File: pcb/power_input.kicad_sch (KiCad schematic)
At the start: 0 parts

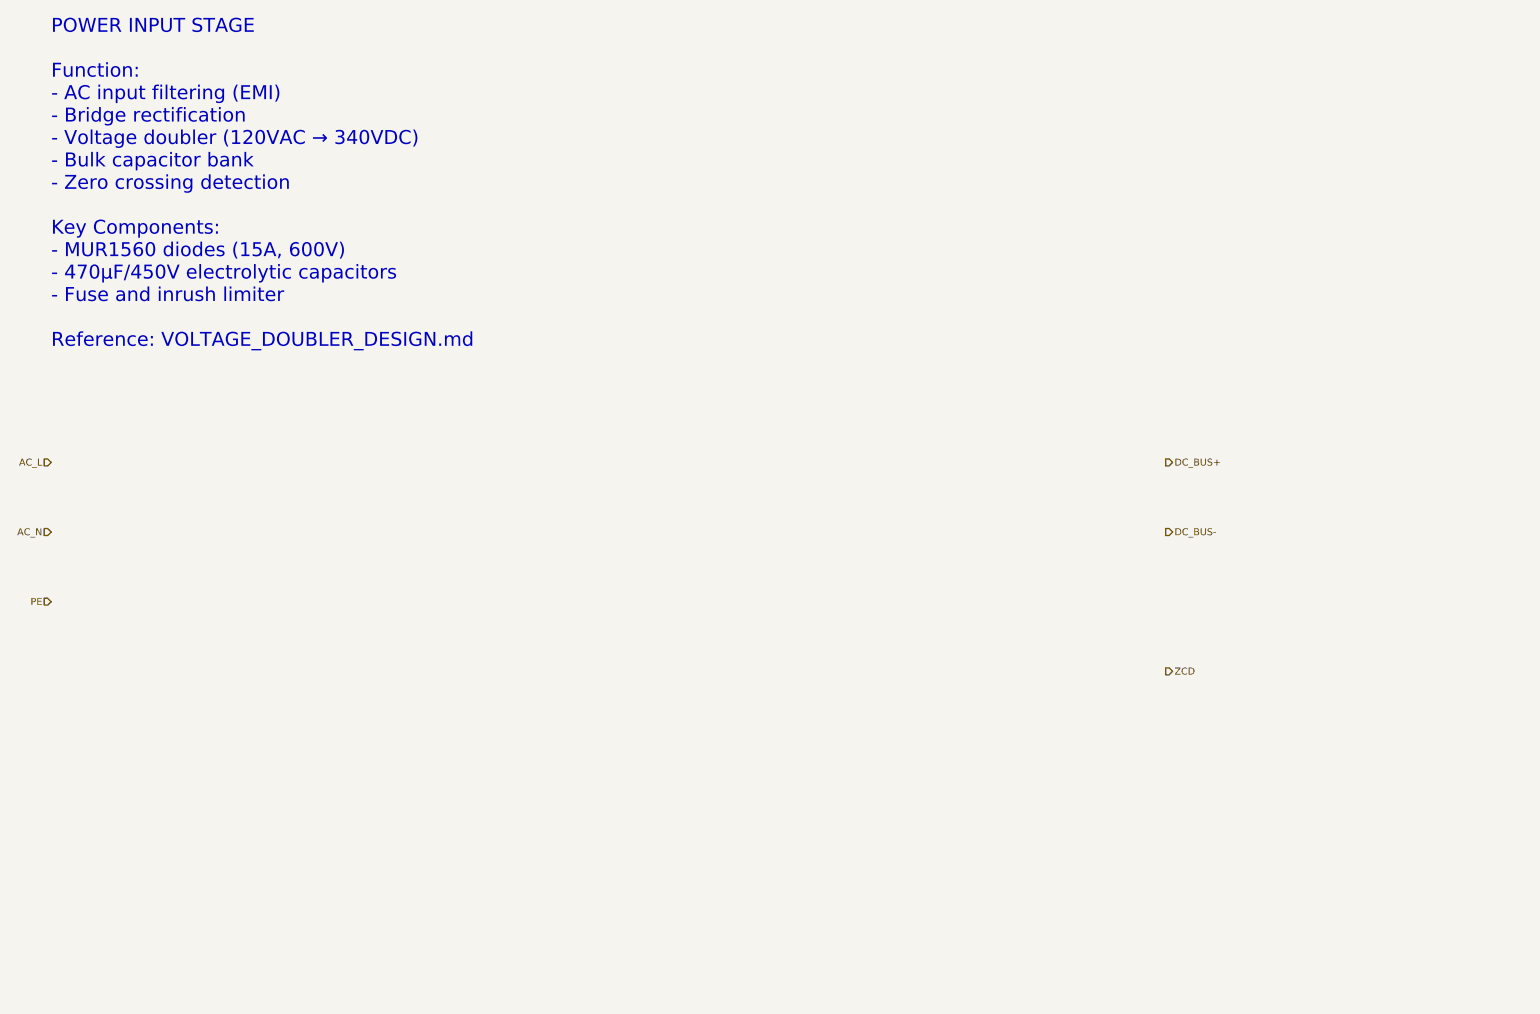
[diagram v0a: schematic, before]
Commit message: feat(pcb): populate all 7 hierarchical schematic sheets with BOM components
Schematics populated:
- half_bridge: IKW40N120H3 IGBTs, UCC21550 gate driver, bootstrap circuit
- power_input: Voltage doubler (MUR1560, 3300uF caps), NTC inrush limiter
- power_management: LMR51430 buck (36V->15V), XC6220 LDO (15V->3.3V)
- safety_interlock: TLV3201 comparators, TPS3823 watchdog, 74HC logic ICs
- sensing: MAX31865 RTD interface, ADUM1250 I2C isolator, CT burden
- mcu: ESP32-S3-WROOM-1-N4, decoupling caps, PWM RC filters, EN circuit
- user_interface: 5x fault LEDs (OCP/OVP/thermal/WDT/master), reset button

All components include MPN properties matching BOM.md specifications.
Pin assignments documented in MCU sheet for firmware reference.
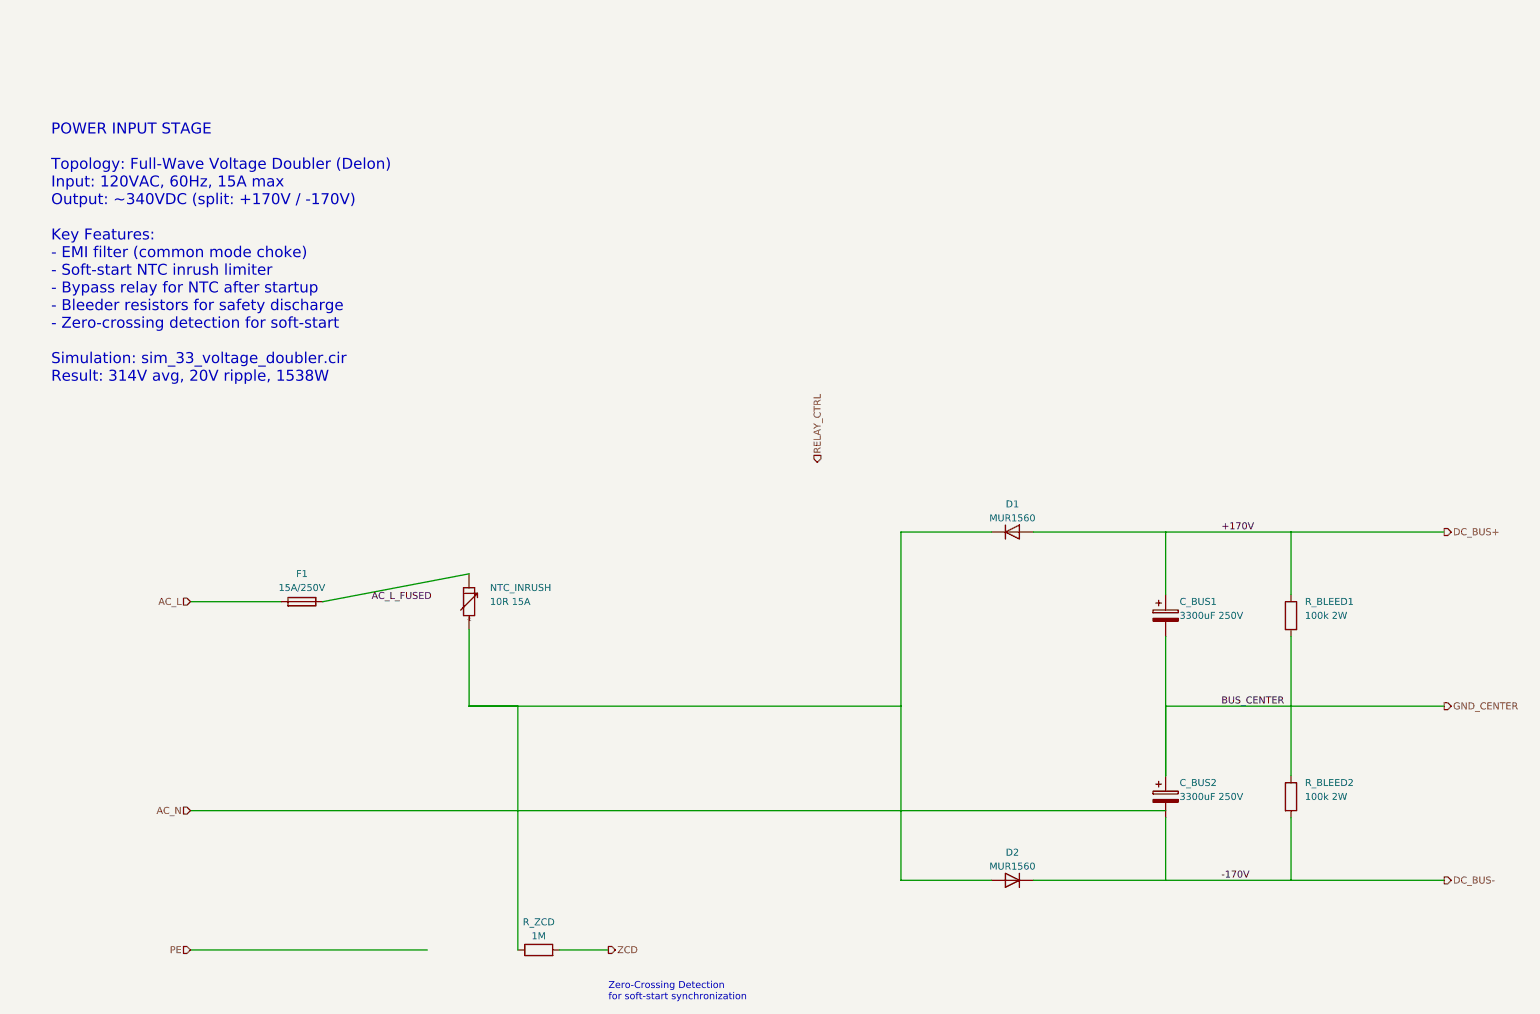
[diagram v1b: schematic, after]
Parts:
- added C_BUS1, C_BUS2: 3300uF 250V, Capacitor_THT:CP_Radial_D35.0mm_P10.00mm_SnapIn, symbol Device:C_Polarized
- added D1, D2: MUR1560, Package_TO_SOT_THT:TO-220-2_Vertical, symbol Device:D
- added F1: 15A/250V, Fuse:Fuse_Holder_5x20mm, symbol Device:Fuse
- added NTC_INRUSH: 10R 15A, Resistor_THT:R_Disc_D15.0mm_W7.0mm_P7.5mm, symbol Device:Thermistor_NTC
- added R_BLEED1, R_BLEED2: 100k 2W, Resistor_SMD:R_2512_6332Metric, symbol Device:R
- added R_ZCD: 1M, Resistor_SMD:R_1206_3216Metric, symbol Device:R
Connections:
- net AC_L: now also F1.1
- net DC_BUS+: now also C_BUS1.1, D1.2 (A), R_BLEED1.1
- net DC_BUS-: now also C_BUS2.2, D2.1 (K), R_BLEED2.2
- net ZCD: now also R_ZCD.2
- new net: F1.2, NTC_INRUSH.1
- new net: D1.1 (K), D2.2 (A), NTC_INRUSH.2, R_ZCD.1
- new net: R_BLEED1.2, R_BLEED2.1
- new net GND_CENTER: C_BUS1.2, C_BUS2.1
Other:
- note added: "POWER INPUT STAGE Topology: Full-Wave Voltage Doubler (Delon) Input: 120VAC, 60Hz, 15A max Output: ~340VDC (split: +170V / -170V) Key Features: - EMI filter (common mode choke) - Soft-start NTC inrush limiter - Bypass relay for NTC after startup - Bleeder resistors for safety discharge - Zero-crossing detection for soft-start Simulation: sim_33_voltage_doubler.cir Result: 314V avg, 20V ripple, 15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"
- note added: "Zero-Crossing Detection for soft-start synchronization"
- note removed: "POWER INPUT STAGE Function: - AC input filtering (EMI) - Bridge rectification - Voltage doubler (120VAC → 340VDC) - Bulk capacitor bank - Zero crossing detection Key Components: - MUR1560 diodes (15A, 600V) - 470µF/450V electrolytic capacitors - Fuse and inrush limiter Reference: VOLTAGE_DOUBLER_DESIGN.md"
- title: Power Input -> Power Input Stage
